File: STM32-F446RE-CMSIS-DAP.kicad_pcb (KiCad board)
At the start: 2 copper layers, 37 parts, among them J1 USB_C_Receptacle_USB2.0, J2 Conn_01x04, J3 Conn_02x04_Odd_Even, J4 Conn_02x05_Odd_Even, J5 Conn_01x04_Female, Y1 26Mhz, Y2 8MHz

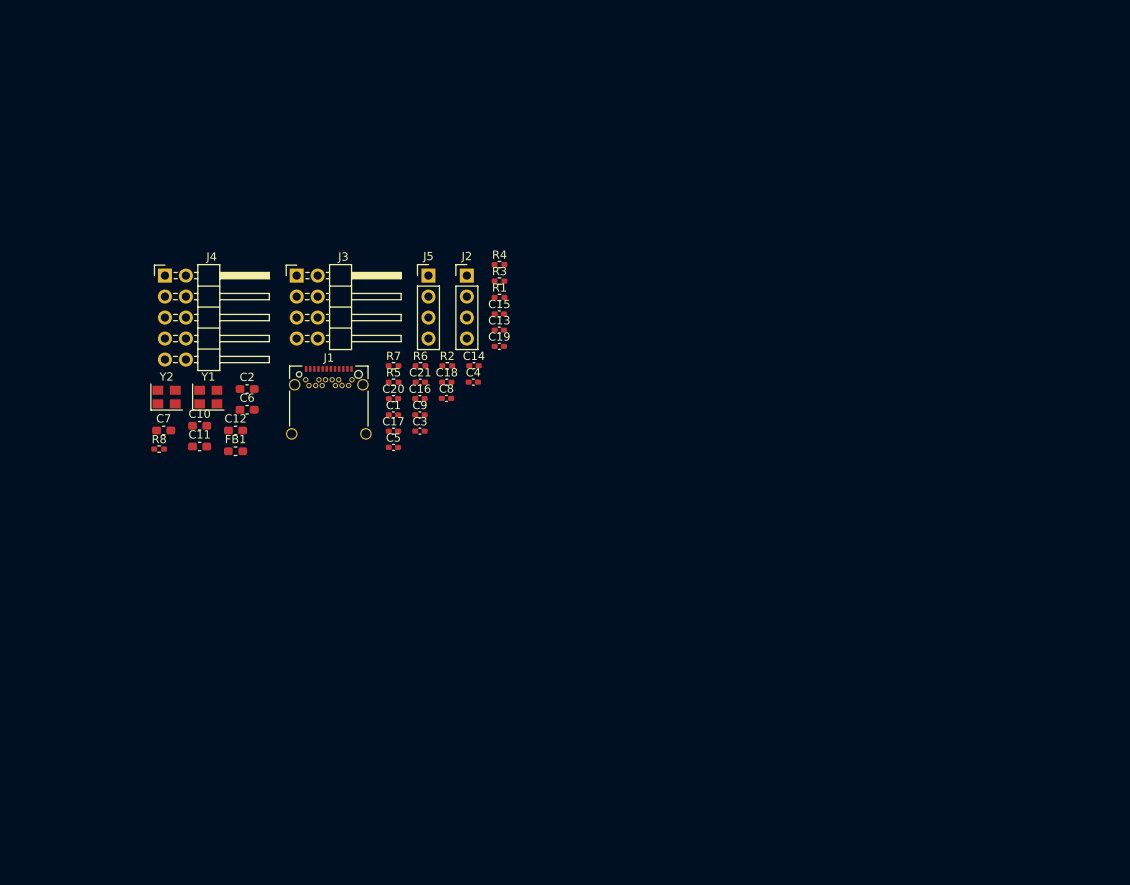
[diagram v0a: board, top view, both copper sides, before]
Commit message: update schematic
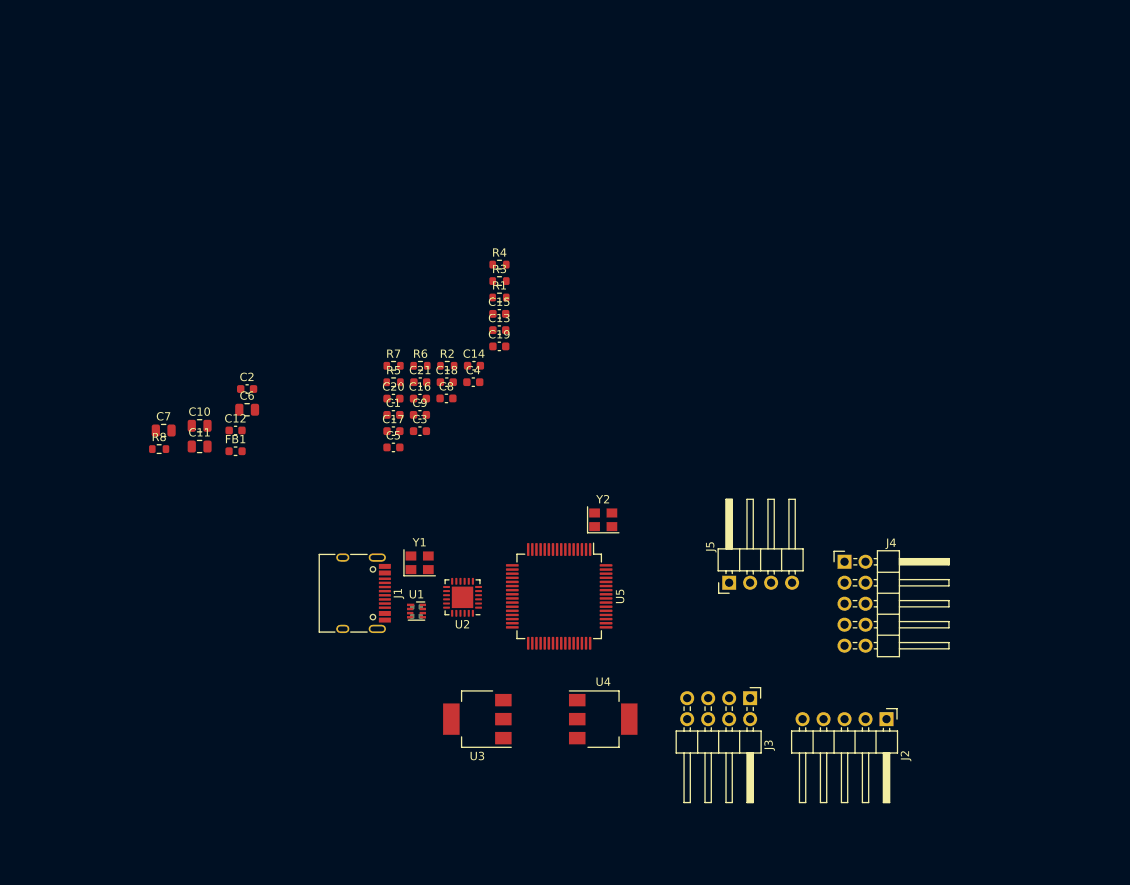
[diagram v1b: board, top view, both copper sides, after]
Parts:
- added R10: 0R0, Resistor_SMD:R_0402_1005Metric, B.Cu at (136.1, 93.0)
- added R9: 0R0, Resistor_SMD:R_0402_1005Metric, B.Cu at (136.1, 91.8)
- added U1: ECMF02-4CMX8, Diode_TVS:Micro_QFN-8_2.5x1.2mm_P0.5mm, F.Cu at (136.1, 92.3)
- added U2: USB3343, Package_DFN_QFN:QFN-24-1EP_4x4mm_P0.5mm_EP2.6x2.6mm, F.Cu at (141.7, 90.7)
- added U3: AMS1117-1.8, Package_TO_SOT_SMD:SOT-223-3_TabPin2, F.Cu at (143.5, 105.4)
- added U4: AMS1117-3.3, Package_TO_SOT_SMD:SOT-223-3_TabPin2, F.Cu at (158.8, 105.4)
- added U5: STM32F446RETx, Package_QFP:LQFP-64_10x10mm_P0.5mm, F.Cu at (153.4, 90.6)
- C1, C13, C14, C15, C16, C17, C18, C19, C20, C21, C3, C4, C5, C8, C9: footprint Capacitor_SMD:C_0402_1005Metric_Pad0.74x0.62mm_HandSolder -> Capacitor_SMD:C_0603_1608Metric
- C10, C11, C6, C7: footprint Capacitor_SMD:C_0603_1608Metric_Pad1.08x0.95mm_HandSolder -> Capacitor_SMD:C_0805_2012Metric
- C12, C2: footprint Capacitor_SMD:C_0603_1608Metric_Pad1.08x0.95mm_HandSolder -> Capacitor_SMD:C_0603_1608Metric
- FB1: footprint Inductor_SMD:L_0603_1608Metric_Pad1.05x0.95mm_HandSolder -> Inductor_SMD:L_0603_1608Metric
- J1: footprint Connector_USB:USB_C_Receptacle_Amphenol_12401548E4-2A_CircularHoles -> Connector_USB:USB_C_Receptacle_HRO_TYPE-C-31-M-12
- J2: value Conn_01x04 -> Conn_01x05; footprint Connector_PinHeader_2.54mm:PinHeader_1x04_P2.54mm_Vertical -> Connector_PinHeader_2.54mm:PinHeader_1x05_P2.54mm_Horizontal
- J5: value Conn_01x04_Female -> Conn_01x04; footprint Connector_PinHeader_2.54mm:PinHeader_1x04_P2.54mm_Vertical -> Connector_PinHeader_2.54mm:PinHeader_1x04_P2.54mm_Horizontal
- R1, R2, R3, R4, R5, R6, R7, R8: footprint Resistor_SMD:R_0402_1005Metric_Pad0.72x0.64mm_HandSolder -> Resistor_SMD:R_0603_1608Metric
- moved J4 89.3 mm to (188.0, 86.4)
- moved J3 75.0 mm to (176.5, 102.9), turned to 270 degrees
- moved J2 73.9 mm to (193.0, 105.4), turned to 270 degrees
- moved Y2 54.9 mm to (158.8, 81.3)
- moved J5 52.0 mm to (174.0, 88.9), turned to 90 degrees
- moved Y1 32.5 mm to (136.5, 86.5)
- moved J1 22.3 mm to (128.3, 90.2), turned to 270 degrees
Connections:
- J1 pad A4: +5VA -> +5V
- J1 pad A9: +5VA -> +5V
- J1 pad B4: +5VA -> +5V
- J1 pad B9: +5VA -> +5V
- J2 pad 1: GND -> +3V3
- J2 pad 2: /I2C_SDA -> /I2C_SCL
- J2 pad 3: /I2C_SCL -> /I2C_SDA
- J2 pad 4: +3V3 -> /I2C_INT
- J3 pad 3: GND -> /SPI_INT
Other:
- net class Default: clearance 0.2 -> 0.127; trace_width 0.25 -> 0.254
- rule trace_clearance: 0.2 -> 0.127

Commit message: Route usb ulpi
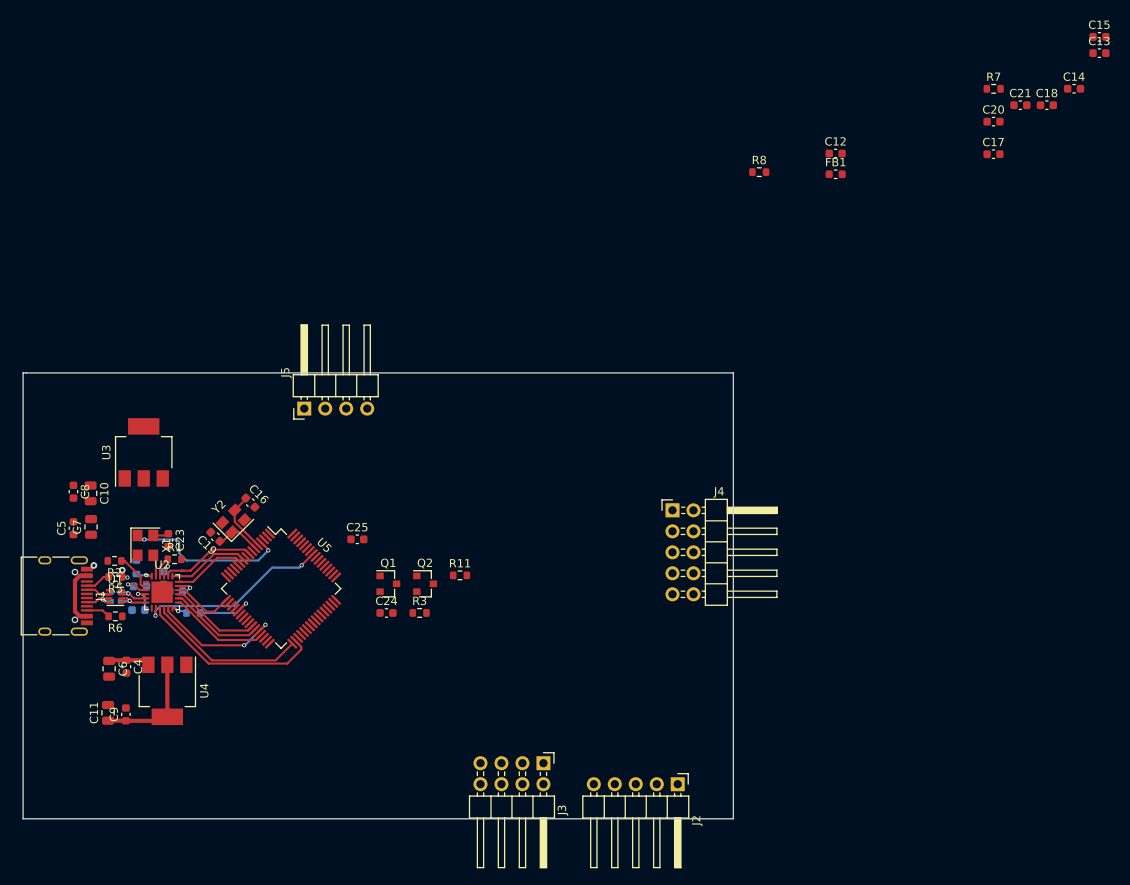
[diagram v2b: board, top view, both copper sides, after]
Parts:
- removed Y1: 26Mhz, Oscillator:Oscillator_SMD_Abracon_ASE-4Pin_3.2x2.5mm
- added C22: 100nF, Capacitor_SMD:C_0603_1608Metric, B.Cu at (107.1, 89.9)
- added C23: 100nF, Capacitor_SMD:C_0603_1608Metric, F.Cu at (106.1, 83.7)
- added C24: 100nF, Capacitor_SMD:C_0603_1608Metric, F.Cu at (132.5, 92.6)
- added C25: 2.2uF, Capacitor_SMD:C_0603_1608Metric, F.Cu at (129.0, 83.6)
- added Q1: BSS83P, Package_TO_SOT_SMD:SOT-23, F.Cu at (132.7, 89.0)
- added Q2: 2N7002, Package_TO_SOT_SMD:SOT-23, F.Cu at (137.2, 89.0)
- added R11: 2K, Resistor_SMD:R_0603_1608Metric, F.Cu at (141.4, 88.0)
- added R12: 22R, Resistor_SMD:R_0603_1608Metric, B.Cu at (109.1, 92.6)
- added X1: SG-5032CAN, Oscillator:Oscillator_SMD_SeikoEpson_SG8002CE-4Pin_3.2x2.5mm, F.Cu at (103.3, 84.4)
- C1, C3: value 12pF -> 100nF; moved to B.Cu
- C2: value 2.2uF -> 100nF; moved to B.Cu
- R2: value 10K -> 810R
- R3: value 1M -> 10K
- R4: moved to B.Cu
- U2: value USB3343 -> USB3315
- U5: value STM32F446RETx -> STM32F205RBTx
- moved C13 80.0 mm to (218.8, 24.8)
- moved C14 80.0 mm to (215.7, 29.1)
- moved C15 80.0 mm to (218.8, 22.8)
- moved C17 80.0 mm to (206.0, 37.0)
- moved C18 80.0 mm to (212.5, 31.1)
- moved C20 80.0 mm to (206.0, 33.1)
- moved C21 80.0 mm to (209.2, 31.1)
- moved FB1 80.0 mm to (186.9, 39.5)
- moved R7 80.0 mm to (206.0, 29.1)
- moved C12 80.0 mm to (186.9, 36.9)
- moved R8 80.0 mm to (177.6, 39.2)
- moved R4 57.2 mm to (102.2, 87.0), turned to 270 degrees
- moved J5 55.6 mm to (122.6, 67.8)
- moved C4 54.3 mm to (101.0, 99.1), turned to 270 degrees
- moved U4 52.9 mm to (106.0, 102.0), turned to 270 degrees
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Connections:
- C1 pad 1: Net-(C1-Pad1) -> +5V
- C2 pad 1: GND -> +3V3
- C2 pad 2: Net-(C2-Pad2) -> GND
- C20 pad 1: Net-(C20-Pad1) -> +3V3
- C3 pad 1: Net-(C3-Pad1) -> +1V8
- J1 pad A6: /USB_DP -> Net-(J1-PadA6)
- J1 pad A7: /USB_DM -> Net-(J1-PadA7)
- R1 pad 1: Net-(R1-Pad1) -> /PHY_RESET
- R1 pad 2: +3V3 -> GND
- R2 pad 1: Net-(C2-Pad2) -> Net-(R2-Pad1)
- R3 pad 1: Net-(C3-Pad1) -> Net-(Q1-Pad1)
- R3 pad 2: Net-(C1-Pad1) -> +3V3
- U1 pad 1: +5VA -> +5V
- U2 pad 1: /ULPI_DIR -> Net-(U2-Pad1)
- U2 pad 11: /ULPI_D6 -> /ULPI_D4
- U2 pad 12: /ULPI_D7 -> Net-(R12-Pad2)
- U2 pad 13: /ULPI_DP -> /ULPI_D3
- U2 pad 14: /ULPI_DM -> /ULPI_D2
- U2 pad 15: +3V3 -> /ULPI_D1
- U2 pad 16: +5V -> /ULPI_D0
- U2 pad 17: Net-(C2-Pad2) -> /PHY_3V3
- U2 pad 18: Net-(R1-Pad1) -> /ULPI_NXT
- U2 pad 19: Net-(R4-Pad2) -> /ULPI_DIR
- U2 pad 2: /ULPI_CK -> Net-(R2-Pad1)
- U2 pad 20: Net-(C1-Pad1) -> /ULPI_STP
- U2 pad 21: Net-(C3-Pad1) -> +1V8
- U2 pad 23: +1V8 -> /PHY_CLK
- U2 pad 24: /ULPI_STP -> Net-(R4-Pad2)
- U2 pad 3: /ULPI_NXP -> +5V
- U2 pad 4: /ULPI_D0 -> +3V3
- U2 pad 5: /ULPI_D1 -> /ULPI_DM
- U2 pad 6: /ULPI_D2 -> /ULPI_DP
- U2 pad 7: /ULPI_D3 -> Net-(U2-Pad7)
- U2 pad 8: /ULPI_D4 -> /ULPI_D7
- U2 pad 9: +3V3 -> /ULPI_D6
- U3 pad 3: Net-(U3-Pad3) -> +3V3
- U5 pad 12: GND -> Net-(U5-Pad12)
- U5 pad 18: GND -> Net-(U5-Pad18)
- U5 pad 30: Net-(C12-Pad1) -> Net-(U5-Pad30)
- U5 pad 31: GND -> Net-(C12-Pad1)
- U5 pad 4: Net-(U5-Pad4) -> /CLK_EN
- U5 pad 47: GND -> Net-(C25-Pad1)
- U5 pad 63: GND -> Net-(U5-Pad63)
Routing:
- net /ULPI_D7: track 0.00 -> 23.4 mm, vias 0 -> 2
- net /ULPI_D6: track 0.00 -> 22.1 mm
- net /CLK_EN: track 0.00 -> 19.7 mm, vias 0 -> 2
- net /ULPI_D5: track 0.00 -> 19.3 mm
- net +3V3: track 0.00 -> 19.1 mm, vias 0 -> 1
- net /ULPI_D4: track 0.00 -> 16.2 mm, vias 0 -> 2
- net +5V: track 0.00 -> 15.4 mm, vias 0 -> 1
- net /ULPI_D3: track 0.00 -> 12.2 mm
- net /ULPI_STP: track 0.00 -> 11.9 mm
- net /ULPI_D2: track 0.00 -> 11.5 mm
- net /ULPI_D1: track 0.00 -> 11.4 mm
- net /ULPI_DIR: track 0.00 -> 10.0 mm
- net /ULPI_NXT: track 0.00 -> 9.99 mm
- net /ULPI_D0: track 0.00 -> 7.85 mm
- net /OSC_IN: track 0.00 -> 7.45 mm
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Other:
- board outline added: 86 x 54 mm
- net class Default: trace_width 0.254 -> 0.127; via_dia 0.8 -> 0.5; via_drill 0.4 -> 0.3
- rule trace_min: 0.2 -> 0.127
- rule via_min_size: 0.4 -> 0.5

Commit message: update route
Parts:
- C12, C13, C14, C15, C17, C18, C21, C24, C25, FB1, Q2, R11, R3, R8: moved to B.Cu
- J5: value Conn_01x04 -> Conn_01x05; footprint Connector_PinHeader_2.54mm:PinHeader_1x04_P2.54mm_Horizontal -> Connector_PinHeader_2.54mm:PinHeader_1x05_P2.54mm_Horizontal
- R5: value 5K1 -> DNP
- R6: value DNP -> 5K1
- moved C15 123.1 mm to (115.1, 89.2), turned to 45 degrees
- moved C13 121.3 mm to (112.9, 84.0), turned to 135 degrees
- moved C21 113.2 mm to (111.5, 88.1), turned to 180 degrees
- moved C14 111.3 mm to (116.9, 80.1), turned to 135 degrees
- moved C17 106.2 mm to (118.8, 97.6), turned to 225 degrees
- moved C18 105.1 mm to (126.4, 91.4), turned to 225 degrees
- moved R7 97.0 mm to (124.7, 82.1), turned to 225 degrees
- moved C20 95.5 mm to (123.2, 80.7), turned to 45 degrees
- moved FB1 90.6 mm to (111.5, 89.6), turned to 180 degrees
- moved C12 87.9 mm to (120.0, 94.1), turned to 45 degrees
- moved R8 80.3 mm to (111.8, 85.1), turned to 315 degrees
- moved J2 66.8 mm to (111.7, 76.9), turned to 90 degrees
- moved R11 43.0 mm to (99.7, 98.5)
- moved Q2 37.8 mm to (99.9, 95.8)
- moved J5 34.7 mm to (123.1, 102.5), turned to 270 degrees
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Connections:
- J5 pad 1: /SWDIO -> GND
- J5 pad 2: /SWCLK -> /NRST
- J5 pad 3: /NRST -> /SWCLK
- J5 pad 4: GND -> /SWDIO
- U5 pad 16: Net-(U5-Pad16) -> /CLK_EN
- U5 pad 4: /CLK_EN -> Net-(U5-Pad4)
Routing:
- net +3V3: track 19.1 -> 45.2 mm, vias 1 -> 5
- net /SWCLK: track 0.00 -> 17.8 mm, vias 0 -> 1
- net /SWDIO: track 0.00 -> 16.9 mm, vias 0 -> 1
- net /I2C_SCL: track 0.00 -> 15.3 mm
- net +1V8: track 2.27 -> 15.9 mm
- net /I2C_SDA: track 0.00 -> 12.4 mm
- net /I2C_INT: track 0.00 -> 11.9 mm
- net /PHY_3V3: track 2.61 -> 13.5 mm, vias 1 -> 2
- net /CLK_EN: track 19.7 -> 13.6 mm
- net +3.3VA: track 0.00 -> 5.39 mm, vias 0 -> 1
- net /NRST: track 0.00 -> 5.03 mm, vias 0 -> 1
- net Net-(C24-Pad1): track 0.00 -> 3.26 mm
- net Net-(C25-Pad1): track 0.00 -> 2.85 mm, vias 0 -> 1
- net Net-(R7-Pad2): track 0.00 -> 2.36 mm
- net Net-(C12-Pad1): track 0.00 -> 2.00 mm, vias 0 -> 1
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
